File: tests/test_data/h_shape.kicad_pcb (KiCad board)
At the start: 2 copper layers, 40 x 40 mm, 0 parts

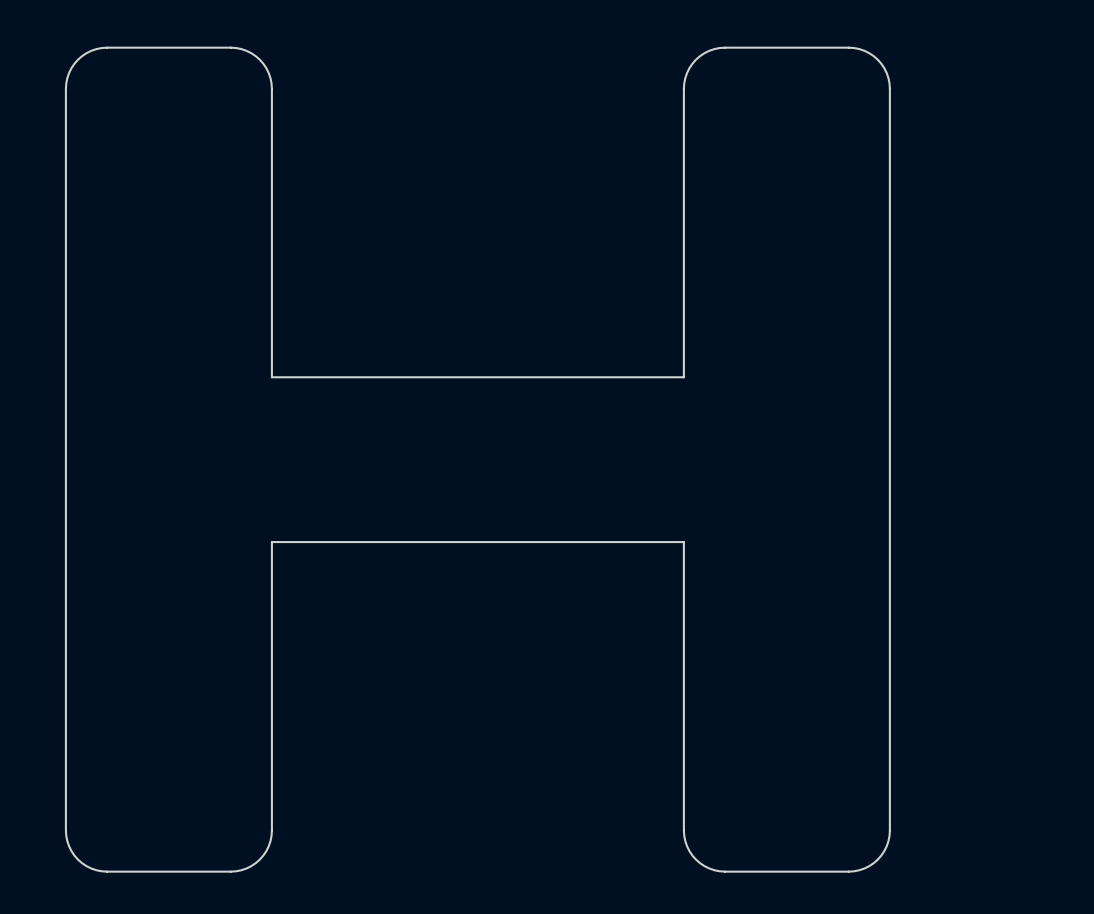
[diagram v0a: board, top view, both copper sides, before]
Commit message: Add trace/pad fold rendering, bend subdivision alignment, and test infrastructure
- Trace mesh: adaptive subdivision at fold boundaries via _compute_fold_crossing_t_values()
  with num_bend_subdivisions parameter to align trace quads with board mesh facets
- Pad mesh: per-vertex region lookup for pads crossing fold boundaries
- Region lookup fallback to last valid region for boundary edge cases
- Normal consistency check (dot product flip detection)
- Z-fighting fix: traces 0.05mm, pads 0.08mm above surface
- Adaptive circle tessellation (~2mm max segment, min 8 segments)
- Variable/formula support for fold angles in markers
- Viewer: variable display labels, traces/pads unchecked by default
- STEP export: 3D component models, stiffener support, pure Python writer
- 33 new tests in test_trace_pad_folds.py (trace/pad/fold + h_shape PCB)
- 10-scene visual test suite (visual_test_phase1.py)
- Updated h_shape.kicad_pcb test data (KiCad 9 format, 8 folds)
- Improvement plan documentation
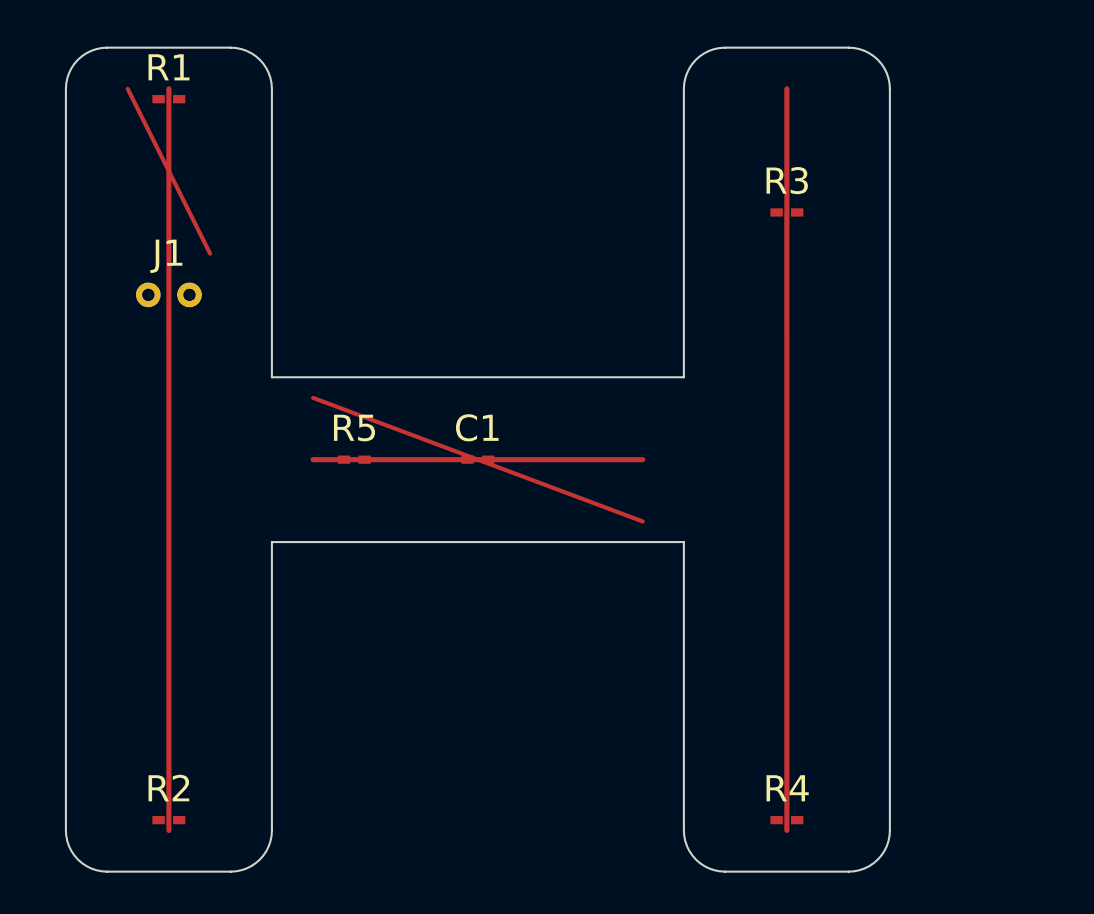
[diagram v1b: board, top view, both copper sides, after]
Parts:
- added C1: 100nF, Capacitor_SMD:C_0402_1005Metric, F.Cu at (20.0, 20.0)
- added J1: Conn, Connector:Conn_01x02, F.Cu at (5.00, 12.0)
- added R1: 10k, Resistor_SMD:R_0402_1005Metric, F.Cu at (5.00, 2.50)
- added R2: 10k, Resistor_SMD:R_0402_1005Metric, F.Cu at (5.00, 37.5)
- added R3: 4.7k, Resistor_SMD:R_0402_1005Metric, F.Cu at (35.0, 8.00)
- added R4: 10k, Resistor_SMD:R_0402_1005Metric, F.Cu at (35.0, 37.5)
- added R5: 1k, Resistor_SMD:R_0402_1005Metric, F.Cu at (14.0, 20.0)
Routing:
- net NET4: track 0.00 -> 47.4 mm
- net NET3: track 0.00 -> 42.0 mm
- net NET2: track 0.00 -> 33.1 mm

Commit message: Update test data files for KiCad 10 format compatibility
KiCad 10 re-saved these files with regenerated UUIDs. All tests pass.
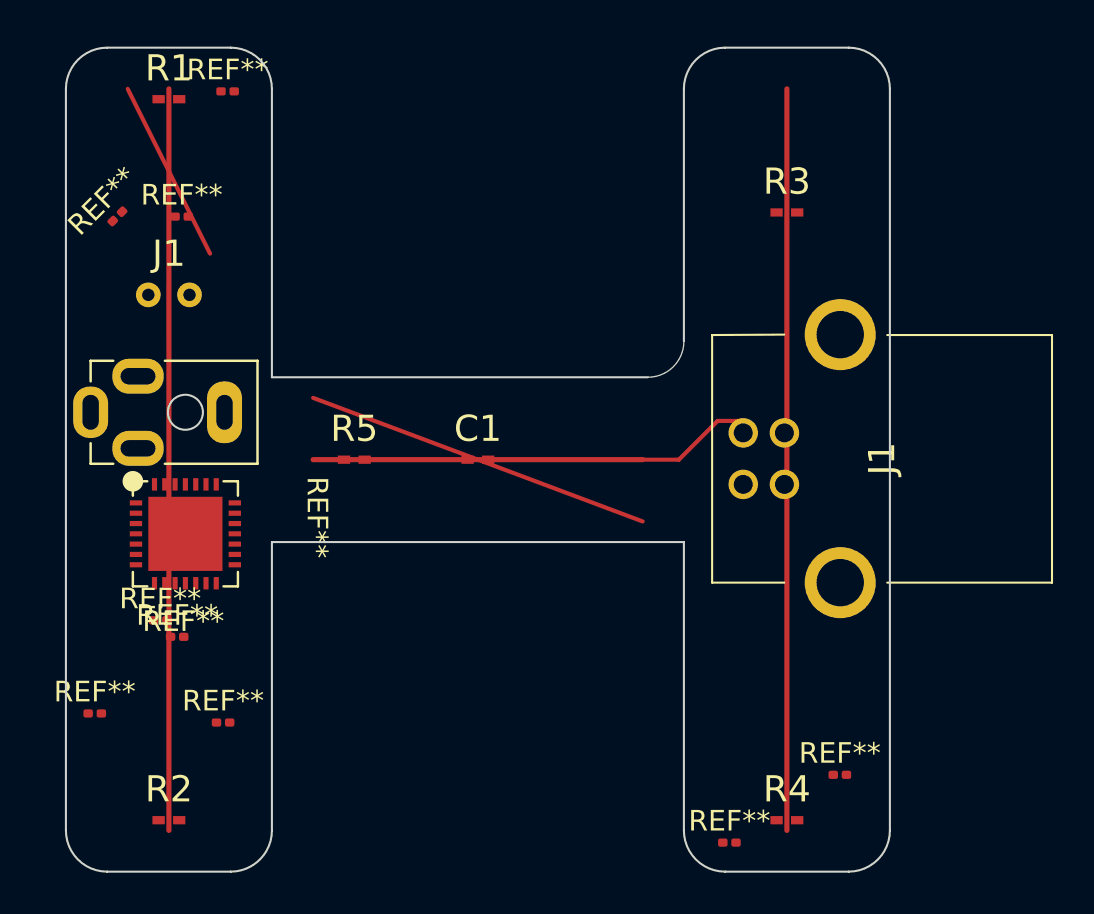
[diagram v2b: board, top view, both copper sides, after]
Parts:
- added J1: SS52300001, 00_custom-footprints:usbB_stewart, F.Cu at (32.9, 21.2)
- added REF**: R_0201_0603Metric, Resistor_SMD:R_0201_0603Metric, F.Cu at (1.40, 32.3)
- added REF**: Jack Socket PJ-210B, 00_custom-footprints:Jack_Socket_PJ-210B, F.Cu at (9.30, 17.7)
- added REF**: R_0201_0603Metric, Resistor_SMD:R_0201_0603Metric, F.Cu at (5.62, 8.20)
- added REF**: R_0201_0603Metric, Resistor_SMD:R_0201_0603Metric, F.Cu at (7.63, 32.8)
- added REF**: R_0201_0603Metric, Resistor_SMD:R_0201_0603Metric, F.Cu at (32.2, 38.6)
- added REF**: R_0201_0603Metric, Resistor_SMD:R_0201_0603Metric, F.Cu at (7.85, 2.12)
- added REF**: R_0201_0603Metric, Resistor_SMD:R_0201_0603Metric, F.Cu at (4.58, 27.8)
- added REF**: R_0201_0603Metric, Resistor_SMD:R_0201_0603Metric, F.Cu at (2.50, 8.19)
- added REF**: R_0201_0603Metric, Resistor_SMD:R_0201_0603Metric, F.Cu at (5.40, 28.6)
- added REF**: RSG28_3P6X3P6_TEX, 00_custom-footprints:ADS1293CISQE, F.Cu at (5.80, 23.6)
- added REF**: R_0201_0603Metric, Resistor_SMD:R_0201_0603Metric, F.Cu at (37.6, 35.3)
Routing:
- net NET2: track 33.1 -> 38.7 mm
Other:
- outline, holes or cut-outs redrawn
- board text added: "ang2=50"
- board text added: "ang=50"
